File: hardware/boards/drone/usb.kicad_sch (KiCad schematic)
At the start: 8 parts, among them J3 USB_C_Receptacle_USB2.0, U7 CYPD3177

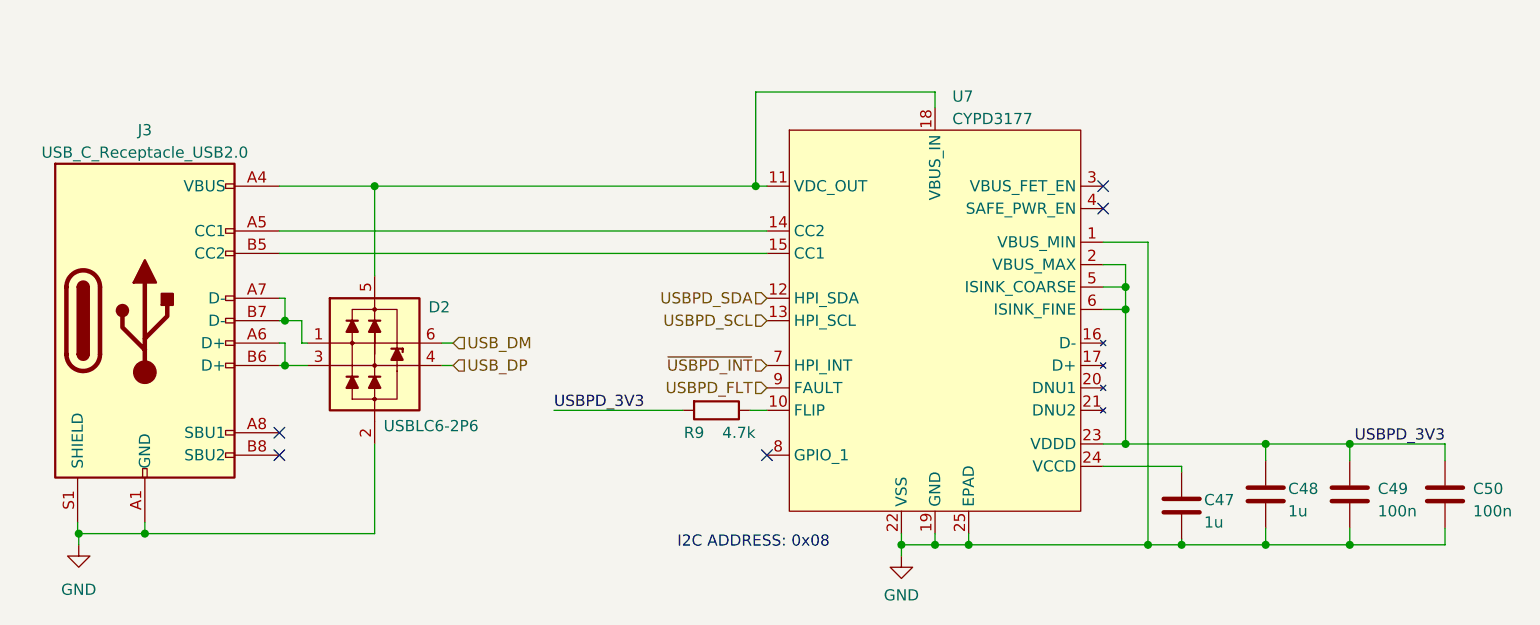
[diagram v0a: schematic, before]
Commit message: Added Power & Charging Subsystems
- Replaced Qi receiver
- Added charge controller
- Added BMS
- Added switch between Qi & USB-PD
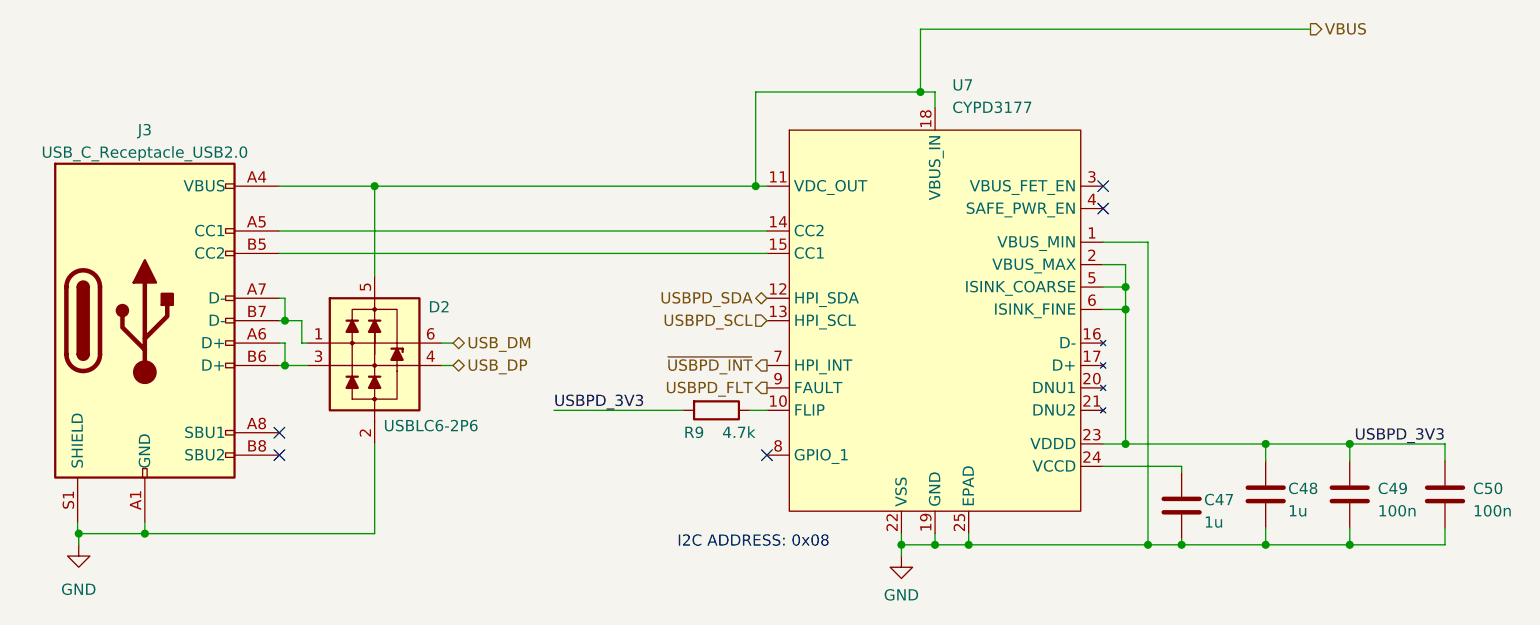
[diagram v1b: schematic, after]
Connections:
- net VBUS: now reaches D2.5 (VP), J3.A4 (VBUS), J3.A9 (VBUS), J3.B4 (VBUS), J3.B9 (VBUS), U7.11 (VDC_OUT), U7.18 (VBUS_IN)
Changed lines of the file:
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@@
   (junction (at 92.075 99.06) (diameter 0) (color 0 0 0 0)
+  )
+  (junction (at 164.084 68.072) (diameter 0) (color 0 0 0 0)
   )
   (junction (at 187.325 92.71) (diameter 0) (color 0 0 0 0)
@@
     (stroke (width 0) (type default))
   )
-  (wire (pts (xy 145.415 68.072) (xy 165.735 68.072))
+  (wire (pts (xy 145.415 68.072) (xy 164.084 68.072))
+    (stroke (width 0) (type default))
+  )
+  (wire (pts (xy 164.084 68.072) (xy 165.735 68.072))
     (stroke (width 0) (type default))
   )
@@
     (stroke (width 0) (type default))
   )
+  (wire (pts (xy 164.084 60.96) (xy 164.084 68.072))
+    (stroke (width 0) (type default))
+  )
   (wire (pts (xy 93.98 96.52) (xy 94.615 96.52))
     (stroke (width 0) (type default))
@@
   )
   (wire (pts (xy 145.415 68.072) (xy 145.415 78.74))
+    (stroke (width 0) (type default))
+  )
+  (wire (pts (xy 208.28 60.96) (xy 164.084 60.96))
     (stroke (width 0) (type default))
   )
@@
     (effects (font (size 1.27 1.27)) (justify left bottom))
   )
-  (hierarchical_label "USB_DP" (shape input) (at 111.125 99.06 0) (fields_autoplaced)
+  (hierarchical_label "USB_DP" (shape bidirectional) (at 111.125 99.06 0) (fields_autoplaced)
     (effects (font (size 1.27 1.27)) (justify left))
   )
-  (hierarchical_label "~{USBPD_INT}" (shape input) (at 146.685 99.06 180) (fields_autoplaced)
+  (hierarchical_label "~{USBPD_INT}" (shape output) (at 146.685 99.06 180) (fields_autoplaced)
     (effects (font (size 1.27 1.27)) (justify right))
   )
-  (hierarchical_label "USB_DM" (shape input) (at 111.125 96.52 0) (fields_autoplaced)
+  (hierarchical_label "USB_DM" (shape bidirectional) (at 111.125 96.52 0) (fields_autoplaced)
     (effects (font (size 1.27 1.27)) (justify left))
   )
-  (hierarchical_label "USBPD_SDA" (shape input) (at 146.685 91.44 180) (fields_autoplaced)
+  (hierarchical_label "USBPD_SDA" (shape bidirectional) (at 146.685 91.44 180) (fields_autoplaced)
     (effects (font (size 1.27 1.27)) (justify right))
   )
-  (hierarchical_label "USBPD_FLT" (shape input) (at 146.685 101.6 180) (fields_autoplaced)
+  (hierarchical_label "VBUS" (shape output) (at 208.28 60.96 0) (fields_autoplaced)
+    (effects (font (size 1.27 1.27)) (justify left))
+  )
+  (hierarchical_label "USBPD_FLT" (shape output) (at 146.685 101.6 180) (fields_autoplaced)
     (effects (font (size 1.27 1.27)) (justify right))
   )
@@
           (reference "C48") (unit 1)
         )
-        (path "/71f6a5b4-1ac6-435b-9486-30b16ab86e62/e763c7b0-792b-4a9b-a885-7de1fed95be3"
+        (path "/71f6a5b4-1ac6-435b-9486-30b16ab86e62/3ebc59d3-e14e-4261-b79d-8c5d78d3b320/092b1374-29af-413a-ad2a-fefc22e5c325"
           (reference "C48") (unit 1)
         )
@@
   (symbol (lib_id "Capstone:CYPD3177-24LQXQ") (at 149.225 99.06 0) (unit 1)
     (in_bom yes) (on_board yes) (dnp no) (fields_autoplaced)
-    (property "Reference" "U7" (at 167.6909 68.58 0)
-      (effects (font (size 1.27 1.27)) (justify left))
-    )
-    (property "Value" "CYPD3177" (at 167.6909 71.12 0)
+    (property "Reference" "U7" (at 167.6909 67.31 0)
+      (effects (font (size 1.27 1.27)) (justify left))
+    )
+    (property "Value" "CYPD3177" (at 167.6909 69.85 0)
       (effects (font (size 1.27 1.27)) (justify left))
     )
@@
           (reference "U7") (unit 1)
         )
-        (path "/71f6a5b4-1ac6-435b-9486-30b16ab86e62/e763c7b0-792b-4a9b-a885-7de1fed95be3"
+        (path "/71f6a5b4-1ac6-435b-9486-30b16ab86e62/3ebc59d3-e14e-4261-b79d-8c5d78d3b320/092b1374-29af-413a-ad2a-fefc22e5c325"
           (reference "U7") (unit 1)
         )
@@
           (reference "R9") (unit 1)
         )
-        (path "/71f6a5b4-1ac6-435b-9486-30b16ab86e62/e763c7b0-792b-4a9b-a885-7de1fed95be3"
+        (path "/71f6a5b4-1ac6-435b-9486-30b16ab86e62/3ebc59d3-e14e-4261-b79d-8c5d78d3b320/092b1374-29af-413a-ad2a-fefc22e5c325"
           (reference "R9") (unit 1)
         )
@@
           (reference "C47") (unit 1)
         )
-        (path "/71f6a5b4-1ac6-435b-9486-30b16ab86e62/e763c7b0-792b-4a9b-a885-7de1fed95be3"
+        (path "/71f6a5b4-1ac6-435b-9486-30b16ab86e62/3ebc59d3-e14e-4261-b79d-8c5d78d3b320/092b1374-29af-413a-ad2a-fefc22e5c325"
           (reference "C47") (unit 1)
         )
@@
           (reference "#PWR035") (unit 1)
         )
-        (path "/71f6a5b4-1ac6-435b-9486-30b16ab86e62/e763c7b0-792b-4a9b-a885-7de1fed95be3"
+        (path "/71f6a5b4-1ac6-435b-9486-30b16ab86e62/3ebc59d3-e14e-4261-b79d-8c5d78d3b320/092b1374-29af-413a-ad2a-fefc22e5c325"
           (reference "#PWR035") (unit 1)
         )
@@
           (reference "C50") (unit 1)
         )
-        (path "/71f6a5b4-1ac6-435b-9486-30b16ab86e62/e763c7b0-792b-4a9b-a885-7de1fed95be3"
+        (path "/71f6a5b4-1ac6-435b-9486-30b16ab86e62/3ebc59d3-e14e-4261-b79d-8c5d78d3b320/092b1374-29af-413a-ad2a-fefc22e5c325"
           (reference "C50") (unit 1)
         )
@@
           (reference "#PWR036") (unit 1)
         )
-        (path "/71f6a5b4-1ac6-435b-9486-30b16ab86e62/e763c7b0-792b-4a9b-a885-7de1fed95be3"
+        (path "/71f6a5b4-1ac6-435b-9486-30b16ab86e62/3ebc59d3-e14e-4261-b79d-8c5d78d3b320/092b1374-29af-413a-ad2a-fefc22e5c325"
           (reference "#PWR036") (unit 1)
         )
@@
           (reference "J3") (unit 1)
         )
-        (path "/71f6a5b4-1ac6-435b-9486-30b16ab86e62/e763c7b0-792b-4a9b-a885-7de1fed95be3"
+        (path "/71f6a5b4-1ac6-435b-9486-30b16ab86e62/3ebc59d3-e14e-4261-b79d-8c5d78d3b320/092b1374-29af-413a-ad2a-fefc22e5c325"
           (reference "J3") (unit 1)
         )
@@
           (reference "C49") (unit 1)
         )
-        (path "/71f6a5b4-1ac6-435b-9486-30b16ab86e62/e763c7b0-792b-4a9b-a885-7de1fed95be3"
+        (path "/71f6a5b4-1ac6-435b-9486-30b16ab86e62/3ebc59d3-e14e-4261-b79d-8c5d78d3b320/092b1374-29af-413a-ad2a-fefc22e5c325"
           (reference "C49") (unit 1)
         )
@@
     (instances
       (project "drone"
-        (path "/71f6a5b4-1ac6-435b-9486-30b16ab86e62/e763c7b0-792b-4a9b-a885-7de1fed95be3"
+        (path "/71f6a5b4-1ac6-435b-9486-30b16ab86e62/3ebc59d3-e14e-4261-b79d-8c5d78d3b320/092b1374-29af-413a-ad2a-fefc22e5c325"
           (reference "D2") (unit 1)
         )
